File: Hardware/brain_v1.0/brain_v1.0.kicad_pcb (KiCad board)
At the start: 2 copper layers, 0 parts

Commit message: started brain layout, can definitely be done in the 100x100 mm space
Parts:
- added C1: 0.1uF, Capacitor_SMD:C_0603_1608Metric, F.Cu at (55.1, 26.8)
- added C2: 1uF, Resistor_SMD:R_0603_1608Metric, F.Cu at (55.1, 29.3)
- added C3: 0.1uF, Capacitor_SMD:C_0603_1608Metric, F.Cu at (55.1, 31.8)
- added C4: 1uF, Resistor_SMD:R_0603_1608Metric, F.Cu at (55.1, 34.3)
- added C5: 0.1uF, Capacitor_SMD:C_0603_1608Metric, F.Cu at (55.1, 36.8)
- added C6: 0.1uF, Capacitor_SMD:C_0603_1608Metric, F.Cu at (55.1, 39.3)
- added C7: 0.1uF, Capacitor_SMD:C_0603_1608Metric, F.Cu at (55.1, 41.9)
- added C8: 0.1uF, Capacitor_SMD:C_0603_1608Metric, F.Cu at (55.1, 44.4)
- added D1: D_Schottky, VS_30BQ015_M3_9AT:VS_30BQ015_M3_9AT, F.Cu at (57.1, 55.8)
- added D2: D_Schottky, VS_30BQ015_M3_9AT:VS_30BQ015_M3_9AT, F.Cu at (57.1, 63.7)
- added H1: MountingHole, MountingHole:MountingHole_3.2mm_M3, F.Cu at (105.2, 52.8)
- added H2: MountingHole, MountingHole:MountingHole_3.2mm_M3, F.Cu at (198.0, 52.8)
- added H3: MountingHole, MountingHole:MountingHole_3.2mm_M3, F.Cu at (105.2, 145.6)
- added H4: MountingHole, MountingHole:MountingHole_3.2mm_M3, F.Cu at (198.0, 145.6)
- added J1: Conn_01x02, Connector_Molex:Molex_KK-254_AE-6410-02A_1x02_P2.54mm_Vertical, F.Cu at (145.6, 145.8)
- added J10: RFID, Connector_Harting:Harting_har-flexicon_14110813001xxx_1x08-MP_P2.54mm_Vertical, F.Cu at (179.8, 145.3)
- added J11: Conn_01x04, Connector_Molex:Molex_KK-254_AE-6410-04A_1x04_P2.54mm_Vertical, F.Cu at (114.8, 145.7)
- added J12: Conn_01x04, Connector_Molex:Molex_KK-254_AE-6410-04A_1x04_P2.54mm_Vertical, F.Cu at (130.5, 145.7)
- added J13: Conn_01x02, Connector_Molex:Molex_KK-254_AE-6410-02A_1x02_P2.54mm_Vertical, F.Cu at (198.1, 78.7)
- added J14: Conn_01x02, Connector_Molex:Molex_KK-254_AE-6410-02A_1x02_P2.54mm_Vertical, F.Cu at (198.1, 71.6)
- added J15: Conn_01x05, Connector_PinHeader_2.54mm:PinHeader_1x05_P2.54mm_Vertical, F.Cu at (103.6, 120.6)
- added J16: Conn_01x02, Connector_Molex:Molex_KK-254_AE-6410-02A_1x02_P2.54mm_Vertical, F.Cu at (198.1, 64.5)
- added J2: Conn_01x02, Connector_Molex:Molex_KK-254_AE-6410-02A_1x02_P2.54mm_Vertical, F.Cu at (156.8, 145.7)
- added J3: Conn_01x03, Connector_Molex:Molex_KK-254_AE-6410-03A_1x03_P2.54mm_Vertical, F.Cu at (198.1, 93.1)
- added J4: JTAG, Connector_PinSocket_2.54mm:PinSocket_1x04_P2.54mm_Vertical, F.Cu at (103.6, 103.8)
- added J5: Conn_01x02, Connector_Molex:Molex_KK-254_AE-6410-02A_1x02_P2.54mm_Vertical, F.Cu at (198.1, 102.2)
- added J6: UART, Connector_PinHeader_2.54mm:PinHeader_1x06_P2.54mm_Vertical, F.Cu at (103.6, 64.8)
- added J7: Conn_01x03, Connector_Molex:Molex_KK-254_AE-6410-03A_1x03_P2.54mm_Vertical, F.Cu at (198.1, 114.1)
- added J8: UART Backup, 61200621621:61200621621, F.Cu at (106.7, 90.4)
- added J9: Conn_01x02, Connector_Molex:Molex_KK-254_AE-6410-02A_1x02_P2.54mm_Vertical, F.Cu at (198.1, 123.2)
- added JP1: SolderJumper_3_Open, Jumper:SolderJumper-3_P1.3mm_Open_RoundedPad1.0x1.5mm, F.Cu at (27.6, 63.4)
- added Q1: BSS138, Package_TO_SOT_SMD:SOT-23, F.Cu at (59.6, 27.8)
- added Q2: BSS138, Package_TO_SOT_SMD:SOT-23, F.Cu at (59.6, 32.2)
- added Q3: SMD-TRANSISTORS-NPN-25V-500MW_SOT-23_, S8050:S8050-SMD, F.Cu at (59.1, 45.5)
- added Q4: SMD-TRANSISTORS-NPN-25V-500MW_SOT-23_, S8050:S8050-SMD, F.Cu at (63.2, 45.5)
- added Q5: BSS138, Package_TO_SOT_SMD:SOT-23, F.Cu at (59.6, 36.7)
- added Q6: BSS138, Package_TO_SOT_SMD:SOT-23, F.Cu at (59.6, 41.1)
- added R1: 100k, Resistor_SMD:R_0805_2012Metric, F.Cu at (27.0, 57.2)
- added R10: 10k, Resistor_SMD:R_1206_3216Metric, F.Cu at (33.5, 50.2)
- added R11: 10k, Resistor_SMD:R_1206_3216Metric, F.Cu at (39.1, 27.2)
- added R12: 10k, Resistor_SMD:R_1206_3216Metric, F.Cu at (39.1, 30.5)
- added R13: 10k, Resistor_SMD:R_1206_3216Metric, F.Cu at (39.1, 33.8)
- added R14: 10k, Resistor_SMD:R_1206_3216Metric, F.Cu at (39.1, 37.0)
- added R15: 10k, Resistor_SMD:R_1206_3216Metric, F.Cu at (39.1, 40.3)
- added R16: 10k, Resistor_SMD:R_1206_3216Metric, F.Cu at (39.1, 43.6)
- added R17: 10k, Resistor_SMD:R_1206_3216Metric, F.Cu at (39.1, 46.9)
- added R18: 10k, Resistor_SMD:R_1206_3216Metric, F.Cu at (39.1, 50.2)
- added R19: 10k, Resistor_SMD:R_1206_3216Metric, F.Cu at (44.7, 27.2)
- added R2: 10k, Resistor_SMD:R_1206_3216Metric, F.Cu at (33.5, 27.2)
- added R20: 10k, Resistor_SMD:R_1206_3216Metric, F.Cu at (44.7, 30.5)
- added R21: 10k, Resistor_SMD:R_1206_3216Metric, F.Cu at (44.7, 33.8)
- added R22: 10k, Resistor_SMD:R_1206_3216Metric, F.Cu at (44.7, 37.0)
- added R23: 10k, Resistor_SMD:R_1206_3216Metric, F.Cu at (44.7, 40.3)
- added R24: 10k, Resistor_SMD:R_1206_3216Metric, F.Cu at (44.7, 43.6)
- added R25: 10k, Resistor_SMD:R_1206_3216Metric, F.Cu at (44.7, 46.9)
- added R26: 10k, Resistor_SMD:R_1206_3216Metric, F.Cu at (44.7, 50.2)
- added R27: 10k, Resistor_SMD:R_1206_3216Metric, F.Cu at (50.3, 27.2)
- added R28: 10k, Resistor_SMD:R_1206_3216Metric, F.Cu at (50.3, 30.5)
- added R29: 10k, Resistor_SMD:R_1206_3216Metric, F.Cu at (50.3, 33.8)
- added R3: 10k, Resistor_SMD:R_1206_3216Metric, F.Cu at (33.5, 30.5)
- added R30: 10k, Resistor_SMD:R_1206_3216Metric, F.Cu at (50.3, 37.0)
- added R31: 10k, Resistor_SMD:R_1206_3216Metric, F.Cu at (50.3, 40.3)
- added R4: 10k, Resistor_SMD:R_1206_3216Metric, F.Cu at (33.5, 33.8)
- added R5: 10k, Resistor_SMD:R_1206_3216Metric, F.Cu at (33.5, 37.0)
- added R6: 10k, Resistor_SMD:R_1206_3216Metric, F.Cu at (33.5, 40.3)
- added R7: 100k, Resistor_SMD:R_0805_2012Metric, F.Cu at (27.0, 60.2)
- added R8: 10k, Resistor_SMD:R_1206_3216Metric, F.Cu at (33.5, 43.6)
- added R9: 10k, Resistor_SMD:R_1206_3216Metric, F.Cu at (33.5, 46.9)
- added SW1: SW_Push, Button_Switch_SMD:SW_SPST_B3U-1000P, F.Cu at (21.9, 57.9)
- added SW2: SW_Push, Button_Switch_SMD:SW_SPST_B3U-1000P, F.Cu at (21.9, 62.3)
- added TP1: TestPoint, TestPoint:TestPoint_Keystone_5010-5014_Multipurpose, F.Cu at (33.2, 54.4)
- added TP2: TestPoint, TestPoint:TestPoint_Keystone_5010-5014_Multipurpose, F.Cu at (33.2, 59.4)
- added TP3: TestPoint, TestPoint:TestPoint_Keystone_5010-5014_Multipurpose, F.Cu at (38.2, 54.4)
- added TP4: TestPoint, TestPoint:TestPoint_Keystone_5010-5014_Multipurpose, F.Cu at (38.2, 59.4)
- added TP5: TestPoint, TestPoint:TestPoint_Keystone_5010-5014_Multipurpose, F.Cu at (43.3, 54.4)
- added TP6: TestPoint, TestPoint:TestPoint_Keystone_5010-5014_Multipurpose, F.Cu at (43.3, 59.4)
- added TP7: TestPoint, TestPoint:TestPoint_Keystone_5010-5014_Multipurpose, F.Cu at (48.3, 54.4)
- added TP8: TestPoint, TestPoint:TestPoint_Keystone_5010-5014_Multipurpose, F.Cu at (48.3, 59.4)
- added U1: ESP32-WROOM-32E 4MB, ESP32-WROOM-32E-N4:ESP32-WROOM-32E-N4, F.Cu at (151.1, 55.4)
- added U2: NAU7802SGI, NAU7802SGI:SOIC127P600X175-16N, F.Cu at (126.0, 132.4)
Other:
- board outline added: 100 x 100 mm
- board text added: "PAWFEAST: FOOD ON DEMAND Group 30 v1.0"

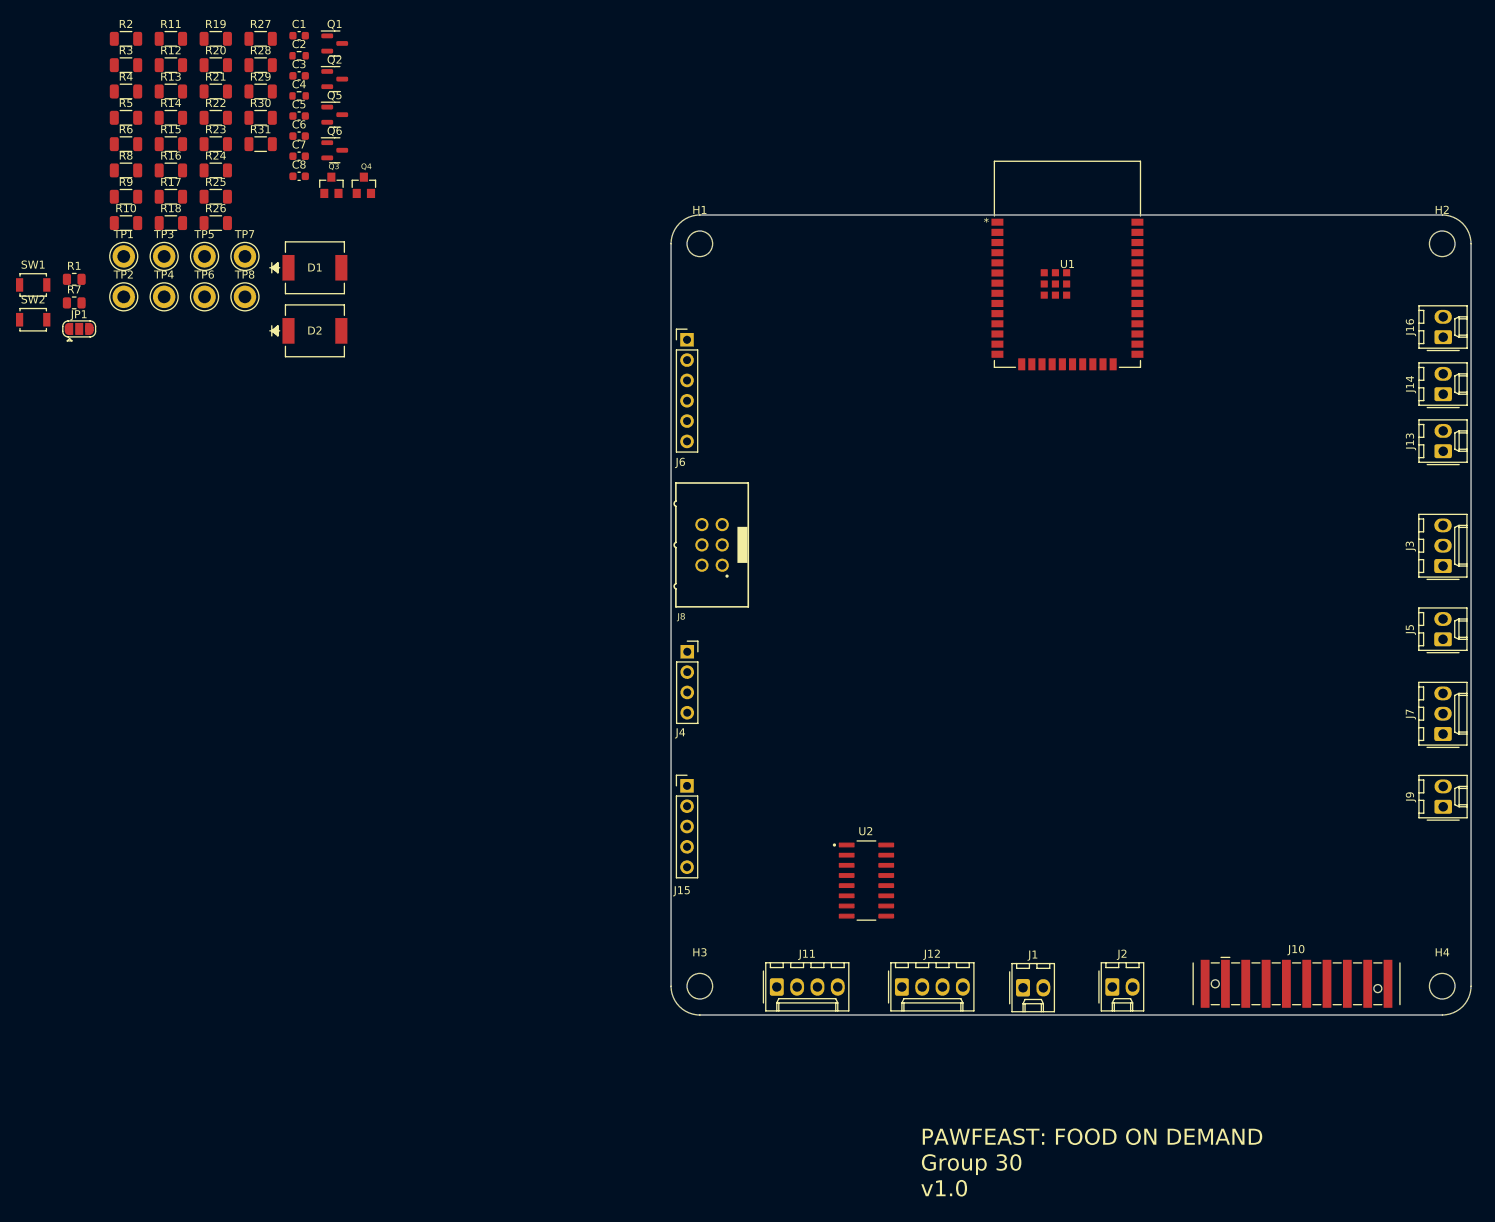
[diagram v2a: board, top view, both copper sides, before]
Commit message: Halfway done with the brain layout--had to fix some issues from the schematic and relink designators. I also added an md file in the Hardware library that specifies how someone can link the Solar Car library and our 3rd party parts (I added both of those folders as well).
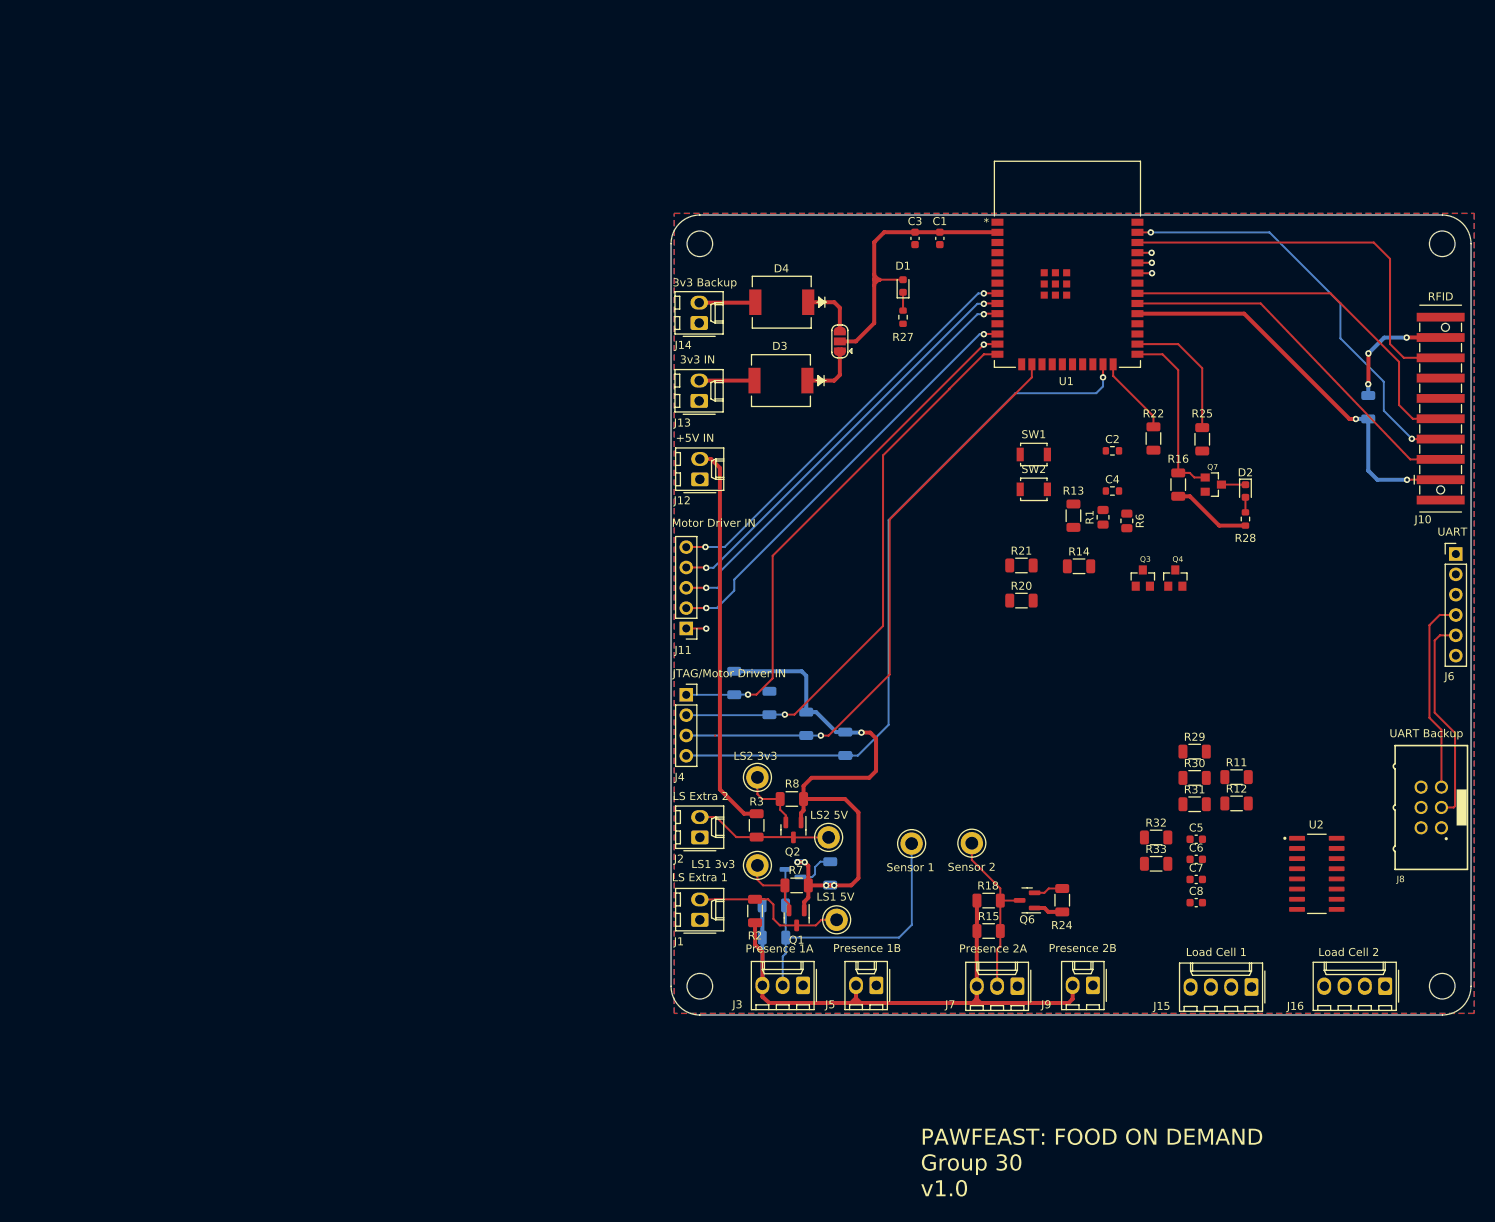
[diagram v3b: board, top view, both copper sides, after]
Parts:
- removed TP6, TP7: TestPoint, TestPoint:TestPoint_Keystone_5010-5014_Multipurpose
- added D3: D_Schottky, VS_30BQ015_M3_9AT:VS_30BQ015_M3_9AT, F.Cu at (115.3, 69.9)
- added D4: D_Schottky, VS_30BQ015_M3_9AT:VS_30BQ015_M3_9AT, F.Cu at (115.4, 60.1)
- added Q7: SMD-TRANSISTORS-NPN-25V-500MW_SOT-23_, S8050:S8050-SMD, F.Cu at (169.4, 82.9)
- added R32: 10k, Resistor_SMD:R_1206_3216Metric, F.Cu at (162.2, 127.0)
- added R33: 10k, Resistor_SMD:R_1206_3216Metric, F.Cu at (162.2, 130.3)
- D1, D2: value D_Schottky -> LED; footprint VS_30BQ015_M3_9AT:VS_30BQ015_M3_9AT -> LED_SMD:LED_0603_1608Metric
- J11: value Conn_01x04 -> Conn_01x05; footprint Connector_Molex:Molex_KK-254_AE-6410-04A_1x04_P2.54mm_Vertical -> Connector_PinHeader_2.54mm:PinHeader_1x05_P2.54mm_Vertical
- J12: value Conn_01x04 -> Conn_01x02; footprint Connector_Molex:Molex_KK-254_AE-6410-04A_1x04_P2.54mm_Vertical -> Connector_Molex:Molex_KK-254_AE-6410-02A_1x02_P2.54mm_Vertical
- J15: value Conn_01x05 -> Conn_01x04; footprint Connector_PinHeader_2.54mm:PinHeader_1x05_P2.54mm_Vertical -> Connector_Molex:Molex_KK-254_AE-6410-04A_1x04_P2.54mm_Vertical
- J16: value Conn_01x02 -> Conn_01x04; footprint Connector_Molex:Molex_KK-254_AE-6410-02A_1x02_P2.54mm_Vertical -> Connector_Molex:Molex_KK-254_AE-6410-04A_1x04_P2.54mm_Vertical
- Q5, R10, R17, R19, R23, R26, R4, R5, R9: moved to B.Cu
- R27, R28: value 10k -> 330; footprint Resistor_SMD:R_1206_3216Metric -> Resistor_SMD:R_0603_1608Metric
- R6: value 10k -> 100k; footprint Resistor_SMD:R_1206_3216Metric -> Resistor_SMD:R_0805_2012Metric
- R7: value 100k -> 10k; footprint Resistor_SMD:R_0805_2012Metric -> Resistor_SMD:R_1206_3216Metric
- moved R11 162.1 mm to (172.3, 119.5)
- moved R12 162.1 mm to (172.3, 122.8)
- moved R19 151.2 mm to (188.8, 73.2), turned to -90 degrees
- moved C8 144.3 mm to (167.2, 135.2)
- moved C5 144.0 mm to (167.2, 127.2)
- moved C6 144.0 mm to (167.2, 129.7)
- moved C7 144.0 mm to (167.2, 132.3)
- moved R29 143.0 mm to (167.1, 116.3)
- moved R30 143.0 mm to (167.1, 119.6)
- moved R31 143.0 mm to (167.1, 122.9)
- moved R15 141.9 mm to (141.3, 138.7)
- moved R24 139.7 mm to (150.5, 134.8), turned to 90 degrees
- moved R28 135.5 mm to (173.4, 87.2), turned to 90 degrees
- moved R2 134.4 mm to (112.1, 136.2), turned to 90 degrees
- moved R6 133.7 mm to (158.6, 87.4), turned to -90 degrees
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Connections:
- D1 pad 2: +3V3 -> /MCU_Power
- D2 pad 2: /3v3 Backup -> Net-(D2-A)
- J11 pad 1: GND -> /GPIO21
- J11 pad 2: Net-(J11-Pin_2) -> /GPIO27
- J11 pad 3: Net-(J11-Pin_3) -> /GPIO25
- J11 pad 4: +3V3 -> /GPIO33
- J12 pad 2: Net-(J12-Pin_2) -> +5V
- J13 pad 2: +5V -> +3V3
- J14 pad 2: +3V3 -> /3v3 Backup
- J15 pad 1: /GPIO33 -> GND
- J15 pad 2: /GPIO32 -> Net-(J15-Pin_2)
- J15 pad 3: /GPIO27 -> Net-(J15-Pin_3)
- J15 pad 4: /GPIO25 -> +3V3
- J16 pad 2: /3v3 Backup -> Net-(J16-Pin_2)
- JP1 pad 1: Net-(D1-K) -> Net-(D3-K)
- JP1 pad 3: Net-(D2-K) -> Net-(D4-K)
- R13 pad 1: +3V3 -> /DTR
- R13 pad 2: /GPIO0 -> Net-(Q3-Pad1)
- R14 pad 1: /DTR -> /RTS
- R14 pad 2: Net-(Q3-Pad1) -> Net-(Q4-Pad1)
- R15 pad 1: /RTS -> +5V
- R15 pad 2: Net-(Q4-Pad1) -> /Presence2
- R16 pad 1: +5V -> +3V3
- R16 pad 2: /Presence2 -> /GPIO0
- R27 pad 1: Net-(J11-Pin_3) -> Net-(D1-K)
- R27 pad 2: Net-(U2-VIN1P) -> GND
- R28 pad 1: Net-(J11-Pin_2) -> +3V3
- R28 pad 2: Net-(U2-VIN1N) -> Net-(D2-A)
- R29 pad 1: Net-(J12-Pin_3) -> Net-(J15-Pin_3)
- R29 pad 2: Net-(U2-VIN2P) -> Net-(U2-VIN1P)
- R30 pad 1: Net-(J12-Pin_2) -> Net-(J15-Pin_2)
- R30 pad 2: Net-(U2-VIN2N) -> Net-(U2-VIN1N)
- R31 pad 1: +3V3 -> Net-(J16-Pin_3)
- R31 pad 2: Net-(U2-REFP) -> Net-(U2-VIN2P)
- R6 pad 2: /TDO -> /CHIP_PU
- R7 pad 2: /CHIP_PU -> /Extra1
- R8 pad 2: /Extra1 -> /Extra2
- R9 pad 2: /Extra2 -> /TDO
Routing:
- net +5V: track 0.00 -> 129.9 mm
- net +3V3: track 0.00 -> 108.0 mm, vias 0 -> 8
- net /TDO: track 0.00 -> 89.0 mm, vias 0 -> 1
- net /TCK: track 0.00 -> 74.8 mm, vias 0 -> 1
- net /TDI: track 0.00 -> 70.1 mm, vias 0 -> 1
- net /TMS: track 0.00 -> 66.0 mm, vias 0 -> 2
- net /GPIO25: track 0.00 -> 54.1 mm, vias 0 -> 2
- net /GPIO27: track 0.00 -> 53.9 mm, vias 0 -> 2
- net /RFID_MOSI: track 0.00 -> 53.6 mm, vias 0 -> 2
- net /GPIO33: track 0.00 -> 52.7 mm, vias 0 -> 2
- net /GPIO32: track 0.00 -> 52.0 mm, vias 0 -> 2
- net /RFID_CS: track 0.00 -> 50.4 mm, vias 0 -> 2
- net /RFID_RST: track 0.00 -> 50.1 mm
- net /RFID_MISO: track 0.00 -> 47.6 mm
- net /RFID_SCK: track 0.00 -> 46.2 mm
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- added copper zone on B.Cu, net GND
- added copper zone on F.Cu, net GND
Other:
- board text added: "+5V"
- board text added: "+5V IN"
- board text added: "1+"
- board text added: "1-"
- board text added: "1A"
- board text added: "2+"
- board text added: "2-"
- board text added: "2A"
- board text added: "3v3"
- board text added: "3v3 Backup"
- board text added: "3v3 IN"
- board text added: "CS"
- board text added: "GND"
- board text added: "JTAG/Motor Driver IN"
- board text added: "LS Extra 1"
- board text added: "LS Extra 2"
- board text added: "LS IN"
- board text added: "LS1 3v3"
- board text added: "LS1 5V"
- board text added: "LS2 3v3"
- board text added: "LS2 5V"
- board text added: "Load Cell 1"
- board text added: "Load Cell 2"
- board text added: "MISO"
- board text added: "MOSI"
- board text added: "Motor Driver IN"
- board text added: "Presence 1A"
- board text added: "Presence 1B"
- board text added: "Presence 2A"
- board text added: "Presence 2B"
- board text added: "RFID"
- board text added: "RST"
- board text added: "RX"
- board text added: "SCK"
- board text added: "Sensor 1"
- board text added: "Sensor 2"
- board text added: "TCK"
- board text added: "TDI"
- board text added: "TDO"
- board text added: "TMS"
- board text added: "TX"
- board text added: "UART"
- board text added: "UART Backup"
